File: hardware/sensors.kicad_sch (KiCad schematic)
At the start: 4 parts, among them U5 BMP390L

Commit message: Updated decoupling caps
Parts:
- removed C26: 10uF, symbol Device:C_Polarized
- added C26: 10uF, symbol Device:C
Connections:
- net GND: now also C26.2
- net VCC: now also C26.1
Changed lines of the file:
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@@
 	(paper "A4")
 	(junction
+		(at 171.45 85.09)
+		(diameter 0)
+		(color 0 0 0 0)
+	)
+	(junction
+		(at 133.35 90.17)
+		(diameter 0)
+		(color 0 0 0 0)
+	)
+	(junction
+		(at 133.35 109.22)
+		(diameter 0)
+		(color 0 0 0 0)
+	)
+	(junction
+		(at 171.45 77.47)
+		(diameter 0)
+		(color 0 0 0 0)
+	)
+	(junction
 		(at 184.15 77.47)
 		(diameter 0)
@@
 	)
 	(junction
-		(at 171.45 85.09)
-		(diameter 0)
-		(color 0 0 0 0)
-	)
-	(junction
-		(at 133.35 90.17)
-		(diameter 0)
-		(color 0 0 0 0)
-	)
-	(junction
-		(at 133.35 109.22)
-		(diameter 0)
-		(color 0 0 0 0)
-	)
-	(junction
-		(at 171.45 77.47)
-		(diameter 0)
-		(color 0 0 0 0)
-	)
-	(junction
 		(at 133.35 106.68)
 		(diameter 0)
@@
 	(wire
 		(pts
-			(xy 184.15 77.47) (xy 199.39 77.47)
+			(xy 184.15 85.09) (xy 198.12 85.09)
 		)
 		(stroke
@@
 	(wire
 		(pts
-			(xy 184.15 85.09) (xy 199.39 85.09)
+			(xy 184.15 77.47) (xy 198.12 77.47)
 		)
 		(stroke
@@
 	)
 	(symbol
-		(lib_id "Device:C_Polarized")
-		(at 199.39 81.28 0)
+		(lib_id "Device:C")
+		(at 198.12 81.28 0)
 		(unit 1)
 		(exclude_from_sim no)
@@
 		(fields_autoplaced yes)
 		(property "Reference" "C26"
-			(at 203.2 79.1209 0)
+			(at 201.93 80.0099 0)
 			(effects
 				(font
@@
 		)
 		(property "Value" "10uF"
-			(at 203.2 81.6609 0)
+			(at 201.93 82.5499 0)
 			(effects
 				(font
@@
 		)
 		(property "Footprint" ""
-			(at 200.3552 85.09 0)
+			(at 199.0852 85.09 0)
 			(effects
 				(font
@@
 		)
 		(property "Datasheet" "~"
-			(at 199.39 81.28 0)
-			(effects
-				(font
-					(size 1.27 1.27)
-				)
-				(hide yes)
-			)
-		)
-		(property "Description" "Polarized capacitor"
-			(at 199.39 81.28 0)
-			(effects
-				(font
-					(size 1.27 1.27)
-				)
-				(hide yes)
-			)
+			(at 198.12 81.28 0)
+			(effects
+				(font
+					(size 1.27 1.27)
+				)
+				(hide yes)
+			)
+		)
+		(property "Description" "Unpolarized capacitor"
+			(at 198.12 81.28 0)
+			(effects
+				(font
+					(size 1.27 1.27)
+				)
+				(hide yes)
+			)
+		)
+		(pin "2"
 		)
 		(pin "1"
 		)
-		(pin "2"
-		)
 		(instances
-			(project "heli_avionics"
+			(project ""
 				(path "/c384ea46-0dfb-4673-b2f4-1f88fafbcaa5/60dd9951-96f3-46dc-a644-dae54ddbd92e"
 					(reference "C26")

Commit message: Assigned footprints for capacitors and inductors
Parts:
- C19, C20, C26: footprint (none) -> Capacitor_SMD:C_0603_1608Metric_Pad1.08x0.95mm_HandSolder
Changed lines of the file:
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@@
 			)
 		)
-		(property "Footprint" ""
+		(property "Footprint" "Capacitor_SMD:C_0603_1608Metric_Pad1.08x0.95mm_HandSolder"
 			(at 199.0852 85.09 0)
 			(effects
@@
 			)
 		)
-		(property "Footprint" ""
+		(property "Footprint" "Capacitor_SMD:C_0603_1608Metric_Pad1.08x0.95mm_HandSolder"
 			(at 185.1152 85.09 0)
 			(effects
@@
 			)
 		)
-		(property "Footprint" ""
+		(property "Footprint" "Capacitor_SMD:C_0603_1608Metric_Pad1.08x0.95mm_HandSolder"
 			(at 172.4152 85.09 0)
 			(effects

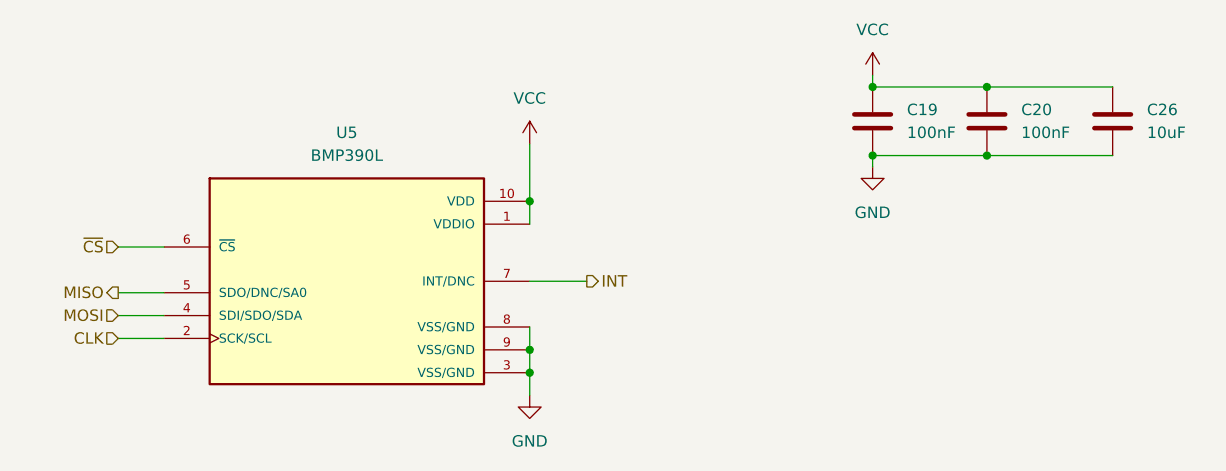
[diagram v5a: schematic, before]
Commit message: Updated decoupling caps to match guidelines from Eric Bogatin
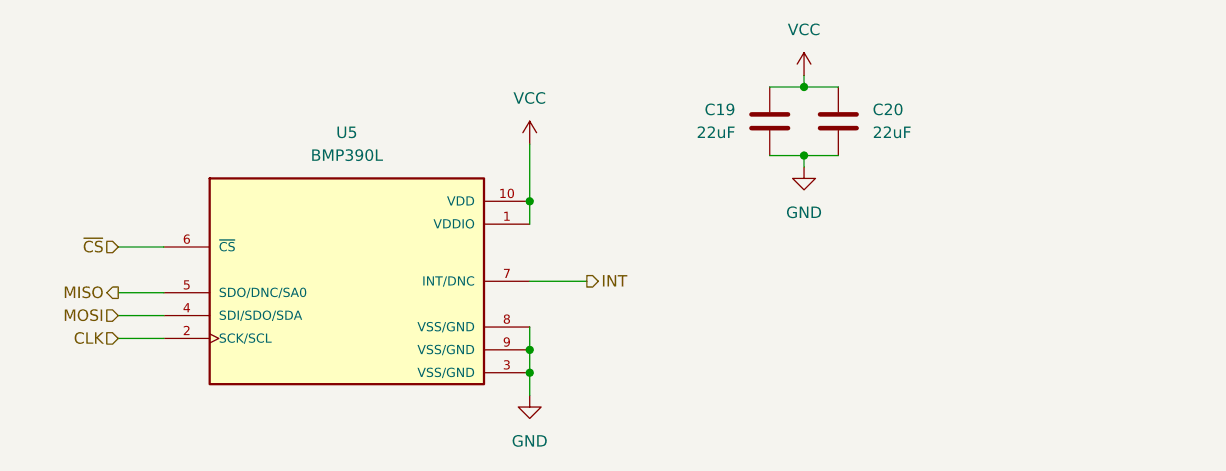
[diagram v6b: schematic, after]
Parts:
- removed C26: 10uF, Capacitor_SMD:C_0603_1608Metric_Pad1.08x0.95mm_HandSolder, symbol Device:C
- C19, C20: value 100nF -> 22uF
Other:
- moved on the sheet: C19, C20
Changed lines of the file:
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@@
 	(paper "A4")
-	(junction
-		(at 171.45 85.09)
-		(diameter 0)
-		(color 0 0 0 0)
-	)
 	(junction
 		(at 133.35 90.17)
@@
 	)
 	(junction
-		(at 171.45 77.47)
+		(at 163.83 85.09)
 		(diameter 0)
 		(color 0 0 0 0)
 	)
 	(junction
-		(at 184.15 77.47)
+		(at 163.83 77.47)
 		(diameter 0)
 		(color 0 0 0 0)
@@
 		(color 0 0 0 0)
 	)
-	(junction
-		(at 184.15 85.09)
-		(diameter 0)
-		(color 0 0 0 0)
-	)
-	(wire
-		(pts
-			(xy 171.45 76.2) (xy 171.45 77.47)
+	(wire
+		(pts
+			(xy 163.83 85.09) (xy 167.64 85.09)
+		)
+		(stroke
+			(width 0)
+			(type default)
+		)
+	)
+	(wire
+		(pts
+			(xy 163.83 76.2) (xy 163.83 77.47)
 		)
 		(stroke
@@
 	(wire
 		(pts
-			(xy 171.45 85.09) (xy 184.15 85.09)
+			(xy 160.02 85.09) (xy 163.83 85.09)
+		)
+		(stroke
+			(width 0)
+			(type default)
+		)
+	)
+	(wire
+		(pts
+			(xy 163.83 77.47) (xy 167.64 77.47)
 		)
 		(stroke
@@
 	(wire
 		(pts
-			(xy 171.45 77.47) (xy 184.15 77.47)
-		)
-		(stroke
-			(width 0)
-			(type default)
-		)
-	)
-	(wire
-		(pts
-			(xy 184.15 85.09) (xy 198.12 85.09)
+			(xy 160.02 77.47) (xy 163.83 77.47)
 		)
 		(stroke
@@
 	(wire
 		(pts
-			(xy 184.15 77.47) (xy 198.12 77.47)
-		)
-		(stroke
-			(width 0)
-			(type default)
-		)
-	)
-	(wire
-		(pts
-			(xy 171.45 86.36) (xy 171.45 85.09)
+			(xy 163.83 86.36) (xy 163.83 85.09)
 		)
 		(stroke
@@
 	(symbol
 		(lib_id "power:VCC")
-		(at 171.45 76.2 0)
+		(at 163.83 76.2 0)
 		(unit 1)
 		(exclude_from_sim no)
@@
 		(fields_autoplaced yes)
 		(property "Reference" "#PWR027"
-			(at 171.45 80.01 0)
+			(at 163.83 80.01 0)
 			(effects
 				(font
@@
 		)
 		(property "Value" "VCC"
-			(at 171.45 71.12 0)
+			(at 163.83 71.12 0)
 			(effects
 				(font
@@
 		)
 		(property "Footprint" ""
-			(at 171.45 76.2 0)
+			(at 163.83 76.2 0)
 			(effects
 				(font
@@
 		)
 		(property "Datasheet" ""
-			(at 171.45 76.2 0)
+			(at 163.83 76.2 0)
 			(effects
 				(font
@@
 		)
 		(property "Description" "Power symbol creates a global label with name \"VCC\""
-			(at 171.45 76.2 0)
+			(at 163.83 76.2 0)
 			(effects
 				(font
@@
 	)
 	(symbol
-		(lib_id "Device:C")
-		(at 198.12 81.28 0)
+		(lib_id "power:GND")
+		(at 163.83 86.36 0)
 		(unit 1)
 		(exclude_from_sim no)
@@
 		(dnp no)
 		(fields_autoplaced yes)
-		(property "Reference" "C26"
-			(at 201.93 80.0099 0)
-			(effects
-				(font
-					(size 1.27 1.27)
-				)
-				(justify left)
-			)
-		)
-		(property "Value" "10uF"
-			(at 201.93 82.5499 0)
-			(effects
-				(font
-					(size 1.27 1.27)
-				)
-				(justify left)
-			)
-		)
-		(property "Footprint" "Capacitor_SMD:C_0603_1608Metric_Pad1.08x0.95mm_HandSolder"
-			(at 199.0852 85.09 0)
-			(effects
-				(font
-					(size 1.27 1.27)
-				)
-				(hide yes)
-			)
-		)
-		(property "Datasheet" "~"
-			(at 198.12 81.28 0)
-			(effects
-				(font
-					(size 1.27 1.27)
-				)
-				(hide yes)
-			)
-		)
-		(property "Description" "Unpolarized capacitor"
-			(at 198.12 81.28 0)
-			(effects
-				(font
-					(size 1.27 1.27)
-				)
-				(hide yes)
-			)
-		)
-		(pin "2"
+		(property "Reference" "#PWR033"
+			(at 163.83 92.71 0)
+			(effects
+				(font
+					(size 1.27 1.27)
+				)
+				(hide yes)
+			)
+		)
+		(property "Value" "GND"
+			(at 163.83 91.44 0)
+			(effects
+				(font
+					(size 1.27 1.27)
+				)
+			)
+		)
+		(property "Footprint" ""
+			(at 163.83 86.36 0)
+			(effects
+				(font
+					(size 1.27 1.27)
+				)
+				(hide yes)
+			)
+		)
+		(property "Datasheet" ""
+			(at 163.83 86.36 0)
+			(effects
+				(font
+					(size 1.27 1.27)
+				)
+				(hide yes)
+			)
+		)
+		(property "Description" "Power symbol creates a global label with name \"GND\" , ground"
+			(at 163.83 86.36 0)
+			(effects
+				(font
+					(size 1.27 1.27)
+				)
+				(hide yes)
+			)
 		)
 		(pin "1"
 		)
 		(instances
-			(project ""
+			(project "heli_avionics"
 				(path "/c384ea46-0dfb-4673-b2f4-1f88fafbcaa5/60dd9951-96f3-46dc-a644-dae54ddbd92e"
-					(reference "C26")
+					(reference "#PWR033")
 					(unit 1)
 				)
@@
 	)
 	(symbol
-		(lib_id "power:GND")
-		(at 171.45 86.36 0)
+		(lib_id "Device:C")
+		(at 167.64 81.28 0)
 		(unit 1)
 		(exclude_from_sim no)
@@
 		(dnp no)
 		(fields_autoplaced yes)
-		(property "Reference" "#PWR033"
-			(at 171.45 92.71 0)
-			(effects
-				(font
-					(size 1.27 1.27)
-				)
-				(hide yes)
-			)
-		)
-		(property "Value" "GND"
-			(at 171.45 91.44 0)
-			(effects
-				(font
-					(size 1.27 1.27)
-				)
-			)
-		)
-		(property "Footprint" ""
-			(at 171.45 86.36 0)
-			(effects
-				(font
-					(size 1.27 1.27)
-				)
-				(hide yes)
-			)
-		)
-		(property "Datasheet" ""
-			(at 171.45 86.36 0)
-			(effects
-				(font
-					(size 1.27 1.27)
-				)
-				(hide yes)
-			)
-		)
-		(property "Description" "Power symbol creates a global label with name \"GND\" , ground"
-			(at 171.45 86.36 0)
-			(effects
-				(font
-					(size 1.27 1.27)
-				)
-				(hide yes)
-			)
-		)
-		(pin "1"
-		)
-		(instances
-			(project "heli_avionics"
-				(path "/c384ea46-0dfb-4673-b2f4-1f88fafbcaa5/60dd9951-96f3-46dc-a644-dae54ddbd92e"
-					(reference "#PWR033")
-					(unit 1)
-				)
-			)
-		)
-	)
-	(symbol
-		(lib_id "Device:C")
-		(at 184.15 81.28 0)
-		(unit 1)
-		(exclude_from_sim no)
-		(in_bom yes)
-		(on_board yes)
-		(dnp no)
-		(fields_autoplaced yes)
 		(property "Reference" "C20"
-			(at 187.96 80.0099 0)
+			(at 171.45 80.0099 0)
 			(effects
 				(font
@@
 			)
 		)
-		(property "Value" "100nF"
-			(at 187.96 82.5499 0)
+		(property "Value" "22uF"
+			(at 171.45 82.5499 0)
 			(effects
 				(font
@@
 		)
 		(property "Footprint" "Capacitor_SMD:C_0603_1608Metric_Pad1.08x0.95mm_HandSolder"
-			(at 185.1152 85.09 0)
+			(at 168.6052 85.09 0)
 			(effects
 				(font
@@
 		)
 		(property "Datasheet" "~"
-			(at 184.15 81.28 0)
+			(at 167.64 81.28 0)
 			(effects
 				(font
@@
 		)
 		(property "Description" "Unpolarized capacitor"
-			(at 184.15 81.28 0)
+			(at 167.64 81.28 0)
 			(effects
 				(font
@@
 	(symbol
 		(lib_id "Device:C")
-		(at 171.45 81.28 0)
+		(at 160.02 81.28 0)
+		(mirror y)
 		(unit 1)
 		(exclude_from_sim no)
@@
 		(on_board yes)
 		(dnp no)
-		(fields_autoplaced yes)
 		(property "Reference" "C19"
-			(at 175.26 80.0099 0)
+			(at 156.21 80.0099 0)
 			(effects
 				(font
@@
 			)
 		)
-		(property "Value" "100nF"
-			(at 175.26 82.5499 0)
+		(property "Value" "22uF"
+			(at 156.21 82.5499 0)
 			(effects
 				(font
@@
 		)
 		(property "Footprint" "Capacitor_SMD:C_0603_1608Metric_Pad1.08x0.95mm_HandSolder"
-			(at 172.4152 85.09 0)
+			(at 159.0548 85.09 0)
 			(effects
 				(font
@@
 		)
 		(property "Datasheet" "~"
-			(at 171.45 81.28 0)
+			(at 160.02 81.28 0)
 			(effects
 				(font
@@
 		)
 		(property "Description" "Unpolarized capacitor"
-			(at 171.45 81.28 0)
-			(effects
-				(font
+			(at 160.02 81.28 0)
+			(effects
+				(font

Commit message: Pressure sensor now uses i2c
Also rewired nrf24 to use the other SPI
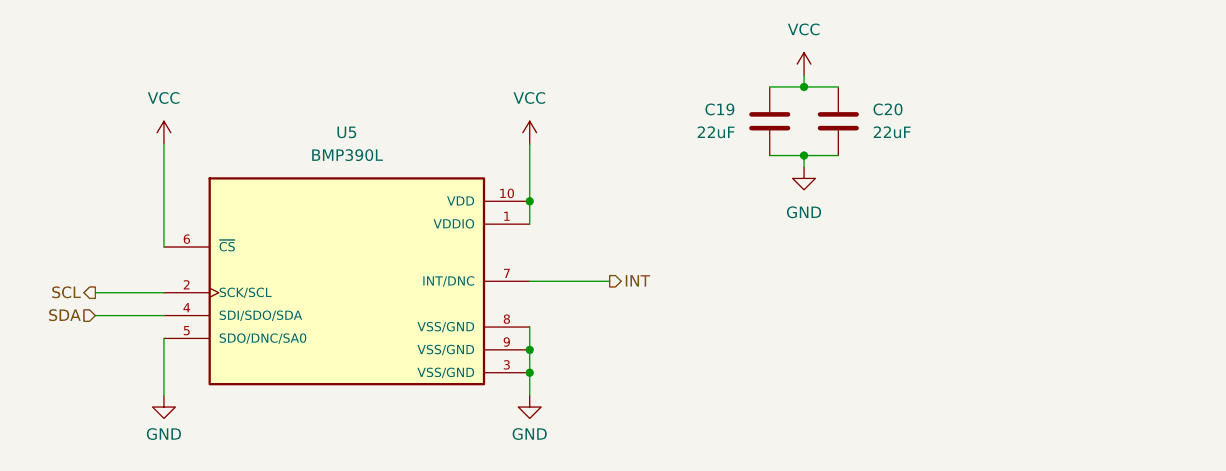
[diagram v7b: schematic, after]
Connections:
- net MISO is gone; now on net GND: U5.5 (SDO/DNC/SA0)
- net ~{CS} is gone; now on net VCC: U5.6 (~{CS})
- net CLK renamed SCL
- net MOSI renamed SDA
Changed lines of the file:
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@@
 	(wire
 		(pts
-			(xy 87.63 95.25) (xy 92.71 95.25)
-		)
-		(stroke
-			(width 0)
-			(type default)
-		)
-	)
-	(wire
-		(pts
-			(xy 87.63 100.33) (xy 92.71 100.33)
+			(xy 92.71 83.82) (xy 92.71 95.25)
+		)
+		(stroke
+			(width 0)
+			(type default)
+		)
+	)
+	(wire
+		(pts
+			(xy 85.09 100.33) (xy 92.71 100.33)
 		)
 		(stroke
@@
 	(wire
 		(pts
-			(xy 87.63 102.87) (xy 92.71 102.87)
+			(xy 85.09 102.87) (xy 92.71 102.87)
 		)
 		(stroke
@@
 	(wire
 		(pts
-			(xy 133.35 99.06) (xy 139.7 99.06)
+			(xy 133.35 99.06) (xy 142.24 99.06)
 		)
 		(stroke
@@
 	(wire
 		(pts
+			(xy 92.71 105.41) (xy 92.71 111.76)
+		)
+		(stroke
+			(width 0)
+			(type default)
+		)
+	)
+	(wire
+		(pts
 			(xy 133.35 104.14) (xy 133.35 106.68)
 		)
@@
 	(wire
 		(pts
-			(xy 87.63 105.41) (xy 92.71 105.41)
-		)
-		(stroke
-			(width 0)
-			(type default)
-		)
-	)
-	(wire
-		(pts
 			(xy 133.35 83.82) (xy 133.35 90.17)
 		)
@@
 		)
 	)
-	(hierarchical_label "~{CS}"
-		(shape input)
-		(at 87.63 95.25 180)
+	(hierarchical_label "INT"
+		(shape output)
+		(at 142.24 99.06 0)
 		(fields_autoplaced yes)
 		(effects
@@
 				(size 1.27 1.27)
 			)
-			(justify right)
-		)
-	)
-	(hierarchical_label "INT"
-		(shape output)
-		(at 139.7 99.06 0)
+			(justify left)
+		)
+	)
+	(hierarchical_label "SDA"
+		(shape input)
+		(at 85.09 102.87 180)
 		(fields_autoplaced yes)
 		(effects
@@
 				(size 1.27 1.27)
 			)
-			(justify left)
-		)
-	)
-	(hierarchical_label "MOSI"
-		(shape input)
-		(at 87.63 102.87 180)
-		(fields_autoplaced yes)
-		(effects
-			(font
-				(size 1.27 1.27)
-			)
 			(justify right)
 		)
 	)
-	(hierarchical_label "MISO"
+	(hierarchical_label "SCL"
 		(shape output)
-		(at 87.63 100.33 180)
-		(fields_autoplaced yes)
-		(effects
-			(font
-				(size 1.27 1.27)
-			)
-			(justify right)
-		)
-	)
-	(hierarchical_label "CLK"
-		(shape input)
-		(at 87.63 105.41 180)
+		(at 85.09 100.33 180)
 		(fields_autoplaced yes)
 		(effects
@@
 	(symbol
 		(lib_id "power:GND")
+		(at 92.71 111.76 0)
+		(unit 1)
+		(exclude_from_sim no)
+		(in_bom yes)
+		(on_board yes)
+		(dnp no)
+		(property "Reference" "#PWR067"
+			(at 92.71 118.11 0)
+			(effects
+				(font
+					(size 1.27 1.27)
+				)
+				(hide yes)
+			)
+		)
+		(property "Value" "GND"
+			(at 92.71 116.078 0)
+			(effects
+				(font
+					(size 1.27 1.27)
+				)
+			)
+		)
+		(property "Footprint" ""
+			(at 92.71 111.76 0)
+			(effects
+				(font
+					(size 1.27 1.27)
+				)
+				(hide yes)
+			)
+		)
+		(property "Datasheet" ""
+			(at 92.71 111.76 0)
+			(effects
+				(font
+					(size 1.27 1.27)
+				)
+				(hide yes)
+			)
+		)
+		(property "Description" "Power symbol creates a global label with name \"GND\" , ground"
+			(at 92.71 111.76 0)
+			(effects
+				(font
+					(size 1.27 1.27)
+				)
+				(hide yes)
+			)
+		)
+		(pin "1"
+		)
+		(instances
+			(project "heli_avionics"
+				(path "/c384ea46-0dfb-4673-b2f4-1f88fafbcaa5/60dd9951-96f3-46dc-a644-dae54ddbd92e"
+					(reference "#PWR067")
+					(unit 1)
+				)
+			)
+		)
+	)
+	(symbol
+		(lib_id "power:GND")
 		(at 163.83 86.36 0)
 		(unit 1)
@@
 	)
 	(symbol
+		(lib_id "power:VCC")
+		(at 92.71 83.82 0)
+		(unit 1)
+		(exclude_from_sim no)
+		(in_bom yes)
+		(on_board yes)
+		(dnp no)
+		(fields_autoplaced yes)
+		(property "Reference" "#PWR020"
+			(at 92.71 87.63 0)
+			(effects
+				(font
+					(size 1.27 1.27)
+				)
+				(hide yes)
+			)
+		)
+		(property "Value" "VCC"
+			(at 92.71 78.74 0)
+			(effects
+				(font
+					(size 1.27 1.27)
+				)
+			)
+		)
+		(property "Footprint" ""
+			(at 92.71 83.82 0)
+			(effects
+				(font
+					(size 1.27 1.27)
+				)
+				(hide yes)
+			)
+		)
+		(property "Datasheet" ""
+			(at 92.71 83.82 0)
+			(effects
+				(font
+					(size 1.27 1.27)
+				)
+				(hide yes)
+			)
+		)
+		(property "Description" "Power symbol creates a global label with name \"VCC\""
+			(at 92.71 83.82 0)
+			(effects
+				(font
+					(size 1.27 1.27)
+				)
+				(hide yes)
+			)
+		)
+		(pin "1"
+		)
+		(instances
+			(project "heli_avionics"
+				(path "/c384ea46-0dfb-4673-b2f4-1f88fafbcaa5/60dd9951-96f3-46dc-a644-dae54ddbd92e"
+					(reference "#PWR020")
+					(unit 1)
+				)
+			)
+		)
+	)
+	(symbol
 		(lib_id "power:GND")
 		(at 133.35 111.76 0)
@@
 		(on_board yes)
 		(dnp no)
-		(fields_autoplaced yes)
 		(property "Reference" "#PWR035"
 			(at 133.35 118.11 0)
@@
 		)
 		(property "Value" "GND"
-			(at 133.35 116.84 0)
-			(effects
-				(font
+			(at 133.35 116.078 0)
+			(effects
+				(font

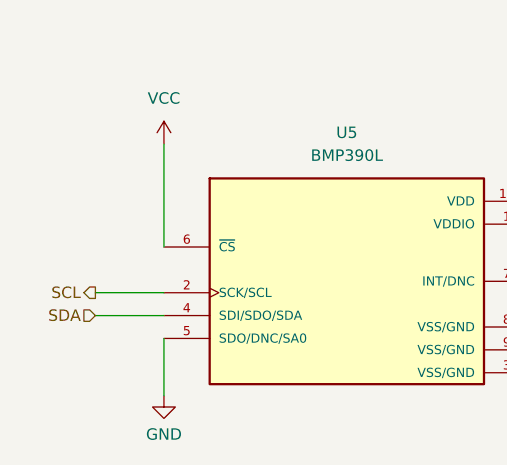
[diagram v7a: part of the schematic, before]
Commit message: Routed most pressure sensor traces
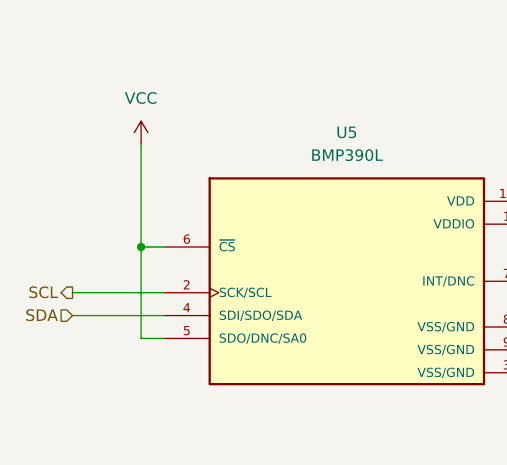
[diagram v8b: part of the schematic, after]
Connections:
- net GND: no longer U5.5 (SDO/DNC/SA0)
- net VCC: now also U5.5 (SDO/DNC/SA0)
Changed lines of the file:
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@@
+	)
+	(junction
+		(at 90.17 95.25)
+		(diameter 0)
+		(color 0 0 0 0)
 	)
 	(junction
@@
 	(wire
 		(pts
-			(xy 92.71 83.82) (xy 92.71 95.25)
-		)
-		(stroke
-			(width 0)
-			(type default)
-		)
-	)
-	(wire
-		(pts
-			(xy 85.09 100.33) (xy 92.71 100.33)
+			(xy 90.17 83.82) (xy 90.17 95.25)
+		)
+		(stroke
+			(width 0)
+			(type default)
+		)
+	)
+	(wire
+		(pts
+			(xy 82.55 100.33) (xy 92.71 100.33)
 		)
 		(stroke
@@
 	(wire
 		(pts
+			(xy 92.71 105.41) (xy 90.17 105.41)
+		)
+		(stroke
+			(width 0)
+			(type default)
+		)
+	)
+	(wire
+		(pts
+			(xy 90.17 95.25) (xy 92.71 95.25)
+		)
+		(stroke
+			(width 0)
+			(type default)
+		)
+	)
+	(wire
+		(pts
 			(xy 163.83 77.47) (xy 167.64 77.47)
 		)
@@
 	(wire
 		(pts
-			(xy 85.09 102.87) (xy 92.71 102.87)
+			(xy 82.55 102.87) (xy 92.71 102.87)
 		)
 		(stroke
@@
 	(wire
 		(pts
-			(xy 92.71 105.41) (xy 92.71 111.76)
-		)
-		(stroke
-			(width 0)
-			(type default)
-		)
-	)
-	(wire
-		(pts
 			(xy 133.35 104.14) (xy 133.35 106.68)
 		)
@@
 		(pts
 			(xy 163.83 86.36) (xy 163.83 85.09)
+		)
+		(stroke
+			(width 0)
+			(type default)
+		)
+	)
+	(wire
+		(pts
+			(xy 90.17 105.41) (xy 90.17 95.25)
 		)
 		(stroke
@@
 	(hierarchical_label "SDA"
 		(shape input)
-		(at 85.09 102.87 180)
+		(at 82.55 102.87 180)
 		(fields_autoplaced yes)
 		(effects
@@
 	(hierarchical_label "SCL"
 		(shape output)
-		(at 85.09 100.33 180)
+		(at 82.55 100.33 180)
 		(fields_autoplaced yes)
 		(effects
@@
 	(symbol
 		(lib_id "power:GND")
-		(at 92.71 111.76 0)
-		(unit 1)
-		(exclude_from_sim no)
-		(in_bom yes)
-		(on_board yes)
-		(dnp no)
-		(property "Reference" "#PWR067"
-			(at 92.71 118.11 0)
-			(effects
-				(font
-					(size 1.27 1.27)
-				)
-				(hide yes)
-			)
-		)
-		(property "Value" "GND"
-			(at 92.71 116.078 0)
-			(effects
-				(font
-					(size 1.27 1.27)
-				)
-			)
-		)
-		(property "Footprint" ""
-			(at 92.71 111.76 0)
-			(effects
-				(font
-					(size 1.27 1.27)
-				)
-				(hide yes)
-			)
-		)
-		(property "Datasheet" ""
-			(at 92.71 111.76 0)
-			(effects
-				(font
-					(size 1.27 1.27)
-				)
-				(hide yes)
-			)
-		)
-		(property "Description" "Power symbol creates a global label with name \"GND\" , ground"
-			(at 92.71 111.76 0)
-			(effects
-				(font
-					(size 1.27 1.27)
-				)
-				(hide yes)
-			)
-		)
-		(pin "1"
-		)
-		(instances
-			(project "heli_avionics"
-				(path "/c384ea46-0dfb-4673-b2f4-1f88fafbcaa5/60dd9951-96f3-46dc-a644-dae54ddbd92e"
-					(reference "#PWR067")
-					(unit 1)
-				)
-			)
-		)
-	)
-	(symbol
-		(lib_id "power:GND")
 		(at 163.83 86.36 0)
 		(unit 1)
@@
 	(symbol
 		(lib_id "power:VCC")
-		(at 92.71 83.82 0)
+		(at 90.17 83.82 0)
 		(unit 1)
 		(exclude_from_sim no)
@@
 		(fields_autoplaced yes)
 		(property "Reference" "#PWR020"
-			(at 92.71 87.63 0)
+			(at 90.17 87.63 0)
 			(effects
 				(font
@@
 		)
 		(property "Value" "VCC"
-			(at 92.71 78.74 0)
+			(at 90.17 78.74 0)
 			(effects
 				(font
@@
 		)
 		(property "Footprint" ""
-			(at 92.71 83.82 0)
+			(at 90.17 83.82 0)
 			(effects
 				(font
@@
 		)
 		(property "Datasheet" ""
-			(at 92.71 83.82 0)
+			(at 90.17 83.82 0)
 			(effects
 				(font
@@
 		)
 		(property "Description" "Power symbol creates a global label with name \"VCC\""
-			(at 92.71 83.82 0)
-			(effects
-				(font
+			(at 90.17 83.82 0)
+			(effects
+				(font
